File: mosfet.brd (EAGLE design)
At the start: 44.1 x 49.5 mm, 14 parts, among them Q1 BC847CSMD, Q2 BC847CSMD, Q3 BC857CSMD, Q4 IRF530, T1 AO3406, T2 AO3407

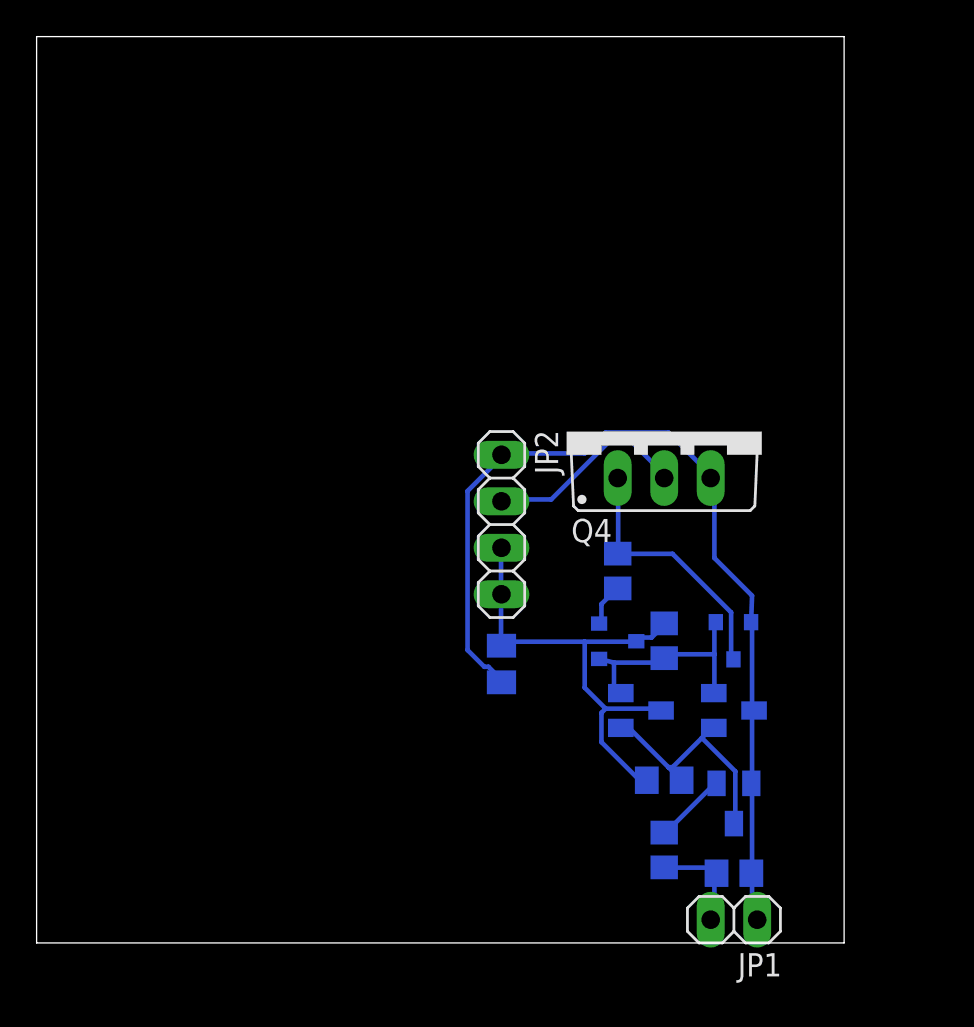
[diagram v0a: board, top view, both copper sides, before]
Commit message: Update mosfet driver to v2
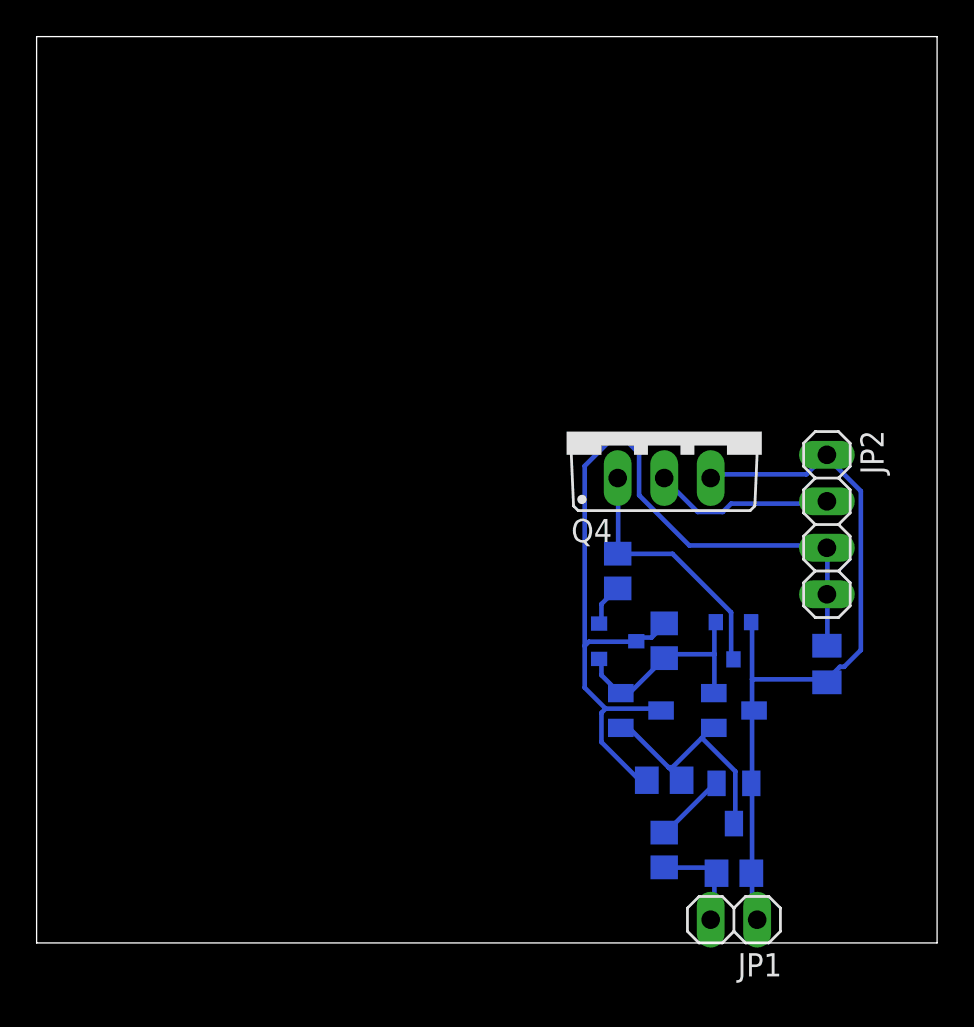
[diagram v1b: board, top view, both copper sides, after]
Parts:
- moved C2 17.8 mm to (43.2, 15.2)
- moved JP2 17.8 mm to (43.2, 22.9)
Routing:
- net N$8: track 27.5 -> 50.1 mm
- net N$3: track 52.5 -> 41.6 mm
- net N$10: track 11.2 -> 9.90 mm
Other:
- board size 44.1 x 49.5 mm -> 49.2 x 49.5 mm

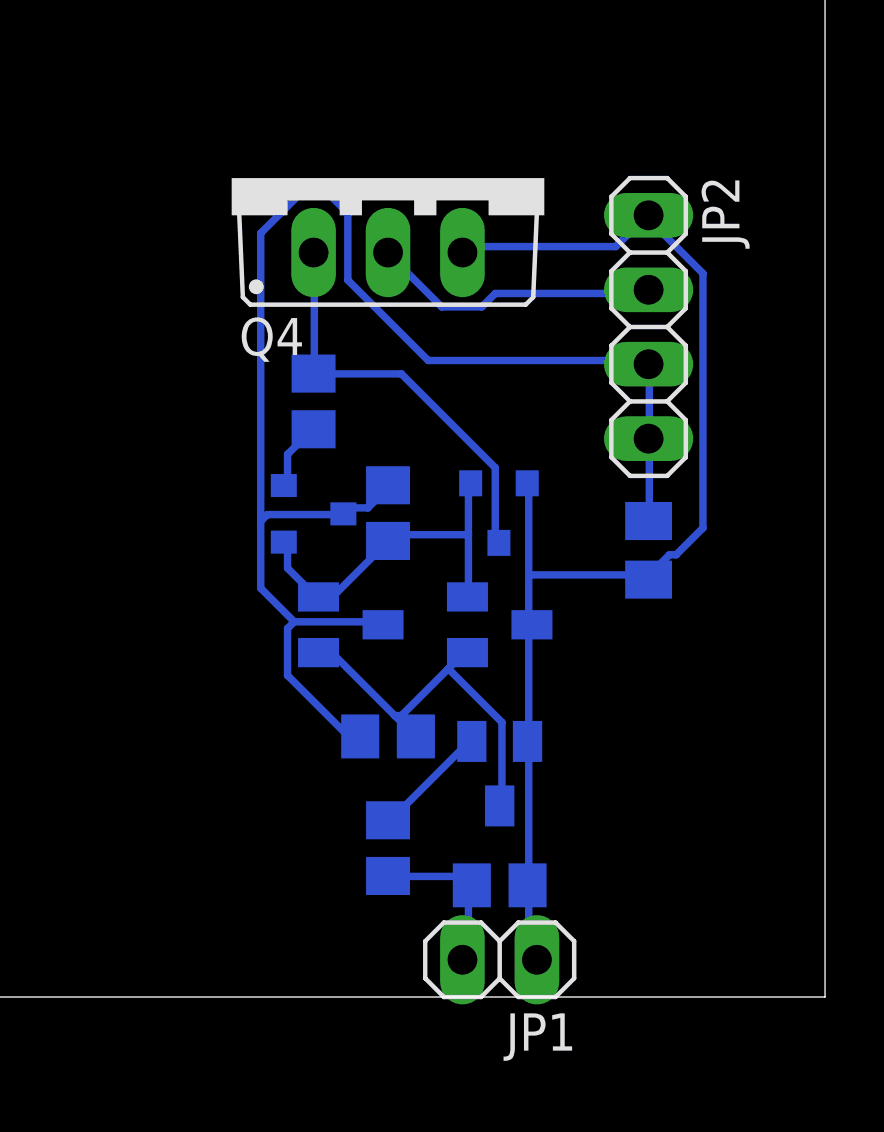
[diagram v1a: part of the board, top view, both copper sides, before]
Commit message: Update mosfet driver to v3
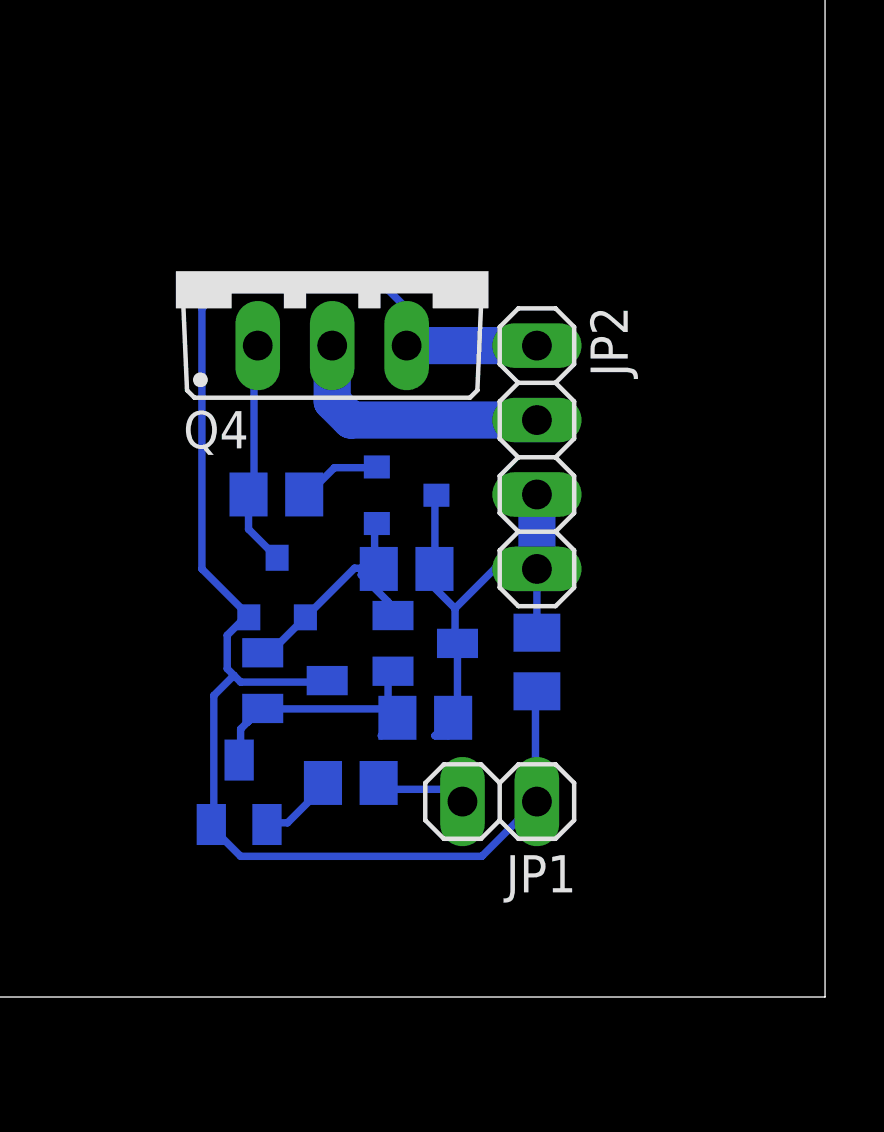
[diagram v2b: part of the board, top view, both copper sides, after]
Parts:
- removed R3: 100k, rcl:R0805
- moved Q2 8.91 mm to (29.2, 6.99), turned to 0 degrees
- moved T1 8.03 mm to (30.5, 14.0), turned to 180 degrees
- moved Q3 7.24 mm to (31.1, 10.8)
- moved JP2 5.85 mm to (39.4, 18.4)
- moved JP1 5.40 mm to (38.1, 6.67)
- moved C2 5.39 mm to (39.4, 11.4)
- moved Q4 3.70 mm to (32.4, 24.8)
- moved R5 3.42 mm to (30.5, 17.1), turned to 180 degrees
- moved T2 3.24 mm to (34.9, 17.1)
- moved Q1 2.62 mm to (35.6, 12.1)
- moved R2 2.56 mm to (33.0, 7.30), turned to 0 degrees
- moved R4 2.01 mm to (34.9, 14.6), turned to 180 degrees
- moved R1 1.42 mm to (35.6, 9.53), turned to 180 degrees
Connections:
- net N$3: no longer R3.1
- net N$5: no longer R3.2
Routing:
- net N$8: track 50.1 -> 19.6 mm
- net N$3: track 41.6 -> 52.5 mm
- net N$1: track 14.3 -> 7.84 mm
- net N$6: track 13.3 -> 10.3 mm
- net N$5: track 5.70 -> 3.26 mm
- net N$7: track 12.4 -> 10.1 mm
- net N$4: track 4.09 -> 2.59 mm
- net N$10: track 9.90 -> 9.15 mm
- net N$2: track 2.35 -> 2.86 mm

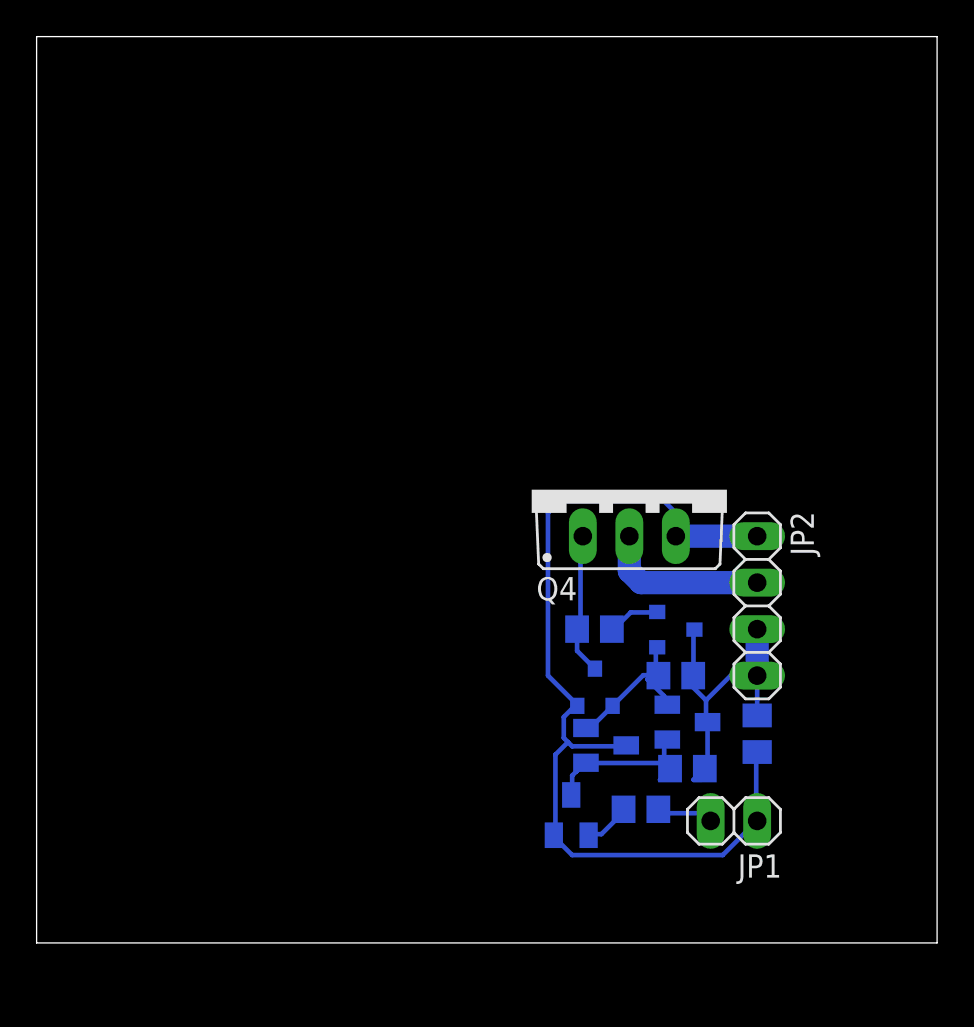
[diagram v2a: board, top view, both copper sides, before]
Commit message: Update mosfet driver to v4
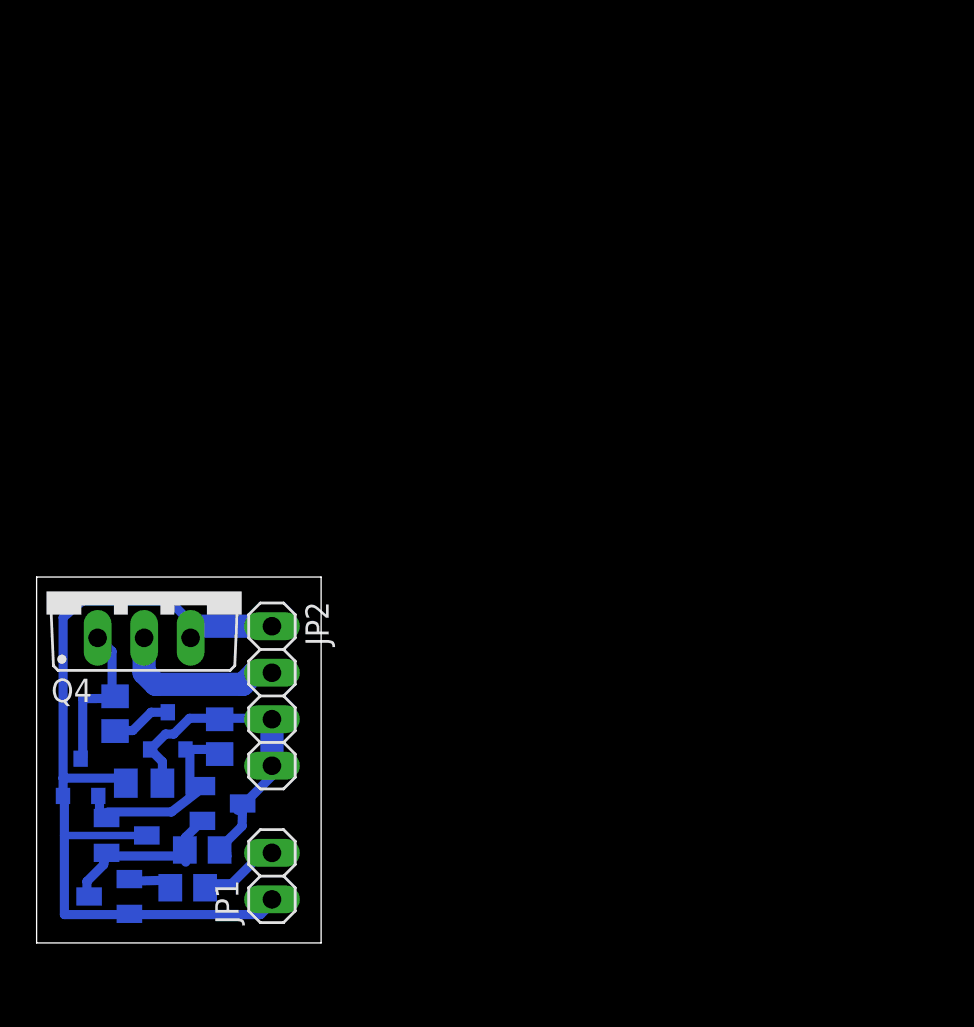
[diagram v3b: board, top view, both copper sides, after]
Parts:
- moved C2 33.6 mm to (5.87, 8.73), turned to 0 degrees
- moved T1 28.5 mm to (2.38, 9.05)
- moved T2 28.3 mm to (7.14, 11.6), turned to 180 degrees
- moved Q4 27.1 mm to (5.87, 19.2)
- moved JP2 27.0 mm to (12.9, 13.5)
- moved R1 26.9 mm to (9.05, 5.08)
- moved Q3 26.7 mm to (4.92, 5.87)
- moved R5 26.6 mm to (4.29, 12.5), turned to 270 degrees
- moved Q1 25.8 mm to (10.2, 7.62)
- moved Q2 25.6 mm to (3.97, 2.54), turned to 270 degrees
- moved JP1 25.4 mm to (12.9, 3.65), turned to 90 degrees
- moved R4 25.1 mm to (10.0, 11.3), turned to 90 degrees
- moved R2 25.1 mm to (8.26, 3.02)
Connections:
- net N$2: now also T2.1; no longer T2.2
- net N$8: now also T2.2; no longer T2.1
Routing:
- net N$7: track 10.1 -> 12.6 mm
- net N$3: track 52.5 -> 50.5 mm
- net N$6: track 10.3 -> 12.0 mm
- net N$5: track 3.26 -> 4.72 mm
- net N$1: track 7.84 -> 8.79 mm
- net N$8: track 19.6 -> 20.4 mm
- net N$4: track 2.59 -> 3.14 mm
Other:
- board size 49.2 x 49.5 mm -> 15.5 x 20 mm

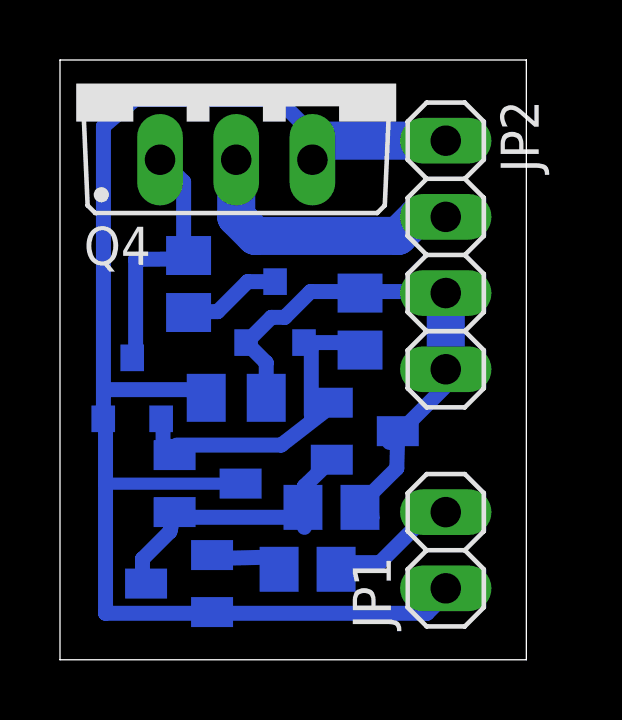
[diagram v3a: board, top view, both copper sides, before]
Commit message: Update mosfet driver to v5
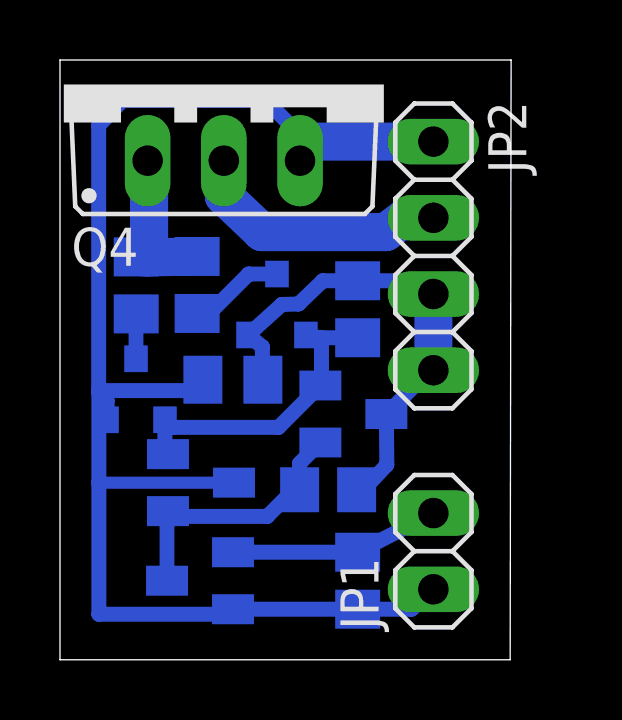
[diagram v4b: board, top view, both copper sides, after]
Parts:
- removed Q2: BC847CSMD, transistor-npn:SOT23
- added R3: 22, rcl:R0805
- added T3: 2N7002E, nxp_60:SOT23
- R2: value 1k -> 100k
- R5: value 10 -> 22
- moved R2 1.71 mm to (9.92, 2.64), turned to 270 degrees
- moved Q1 0.69 mm to (9.78, 8.19)
- moved C2 0.61 mm to (5.76, 9.33)
- moved R1 0.60 mm to (8.94, 5.67)
- moved R4 0.42 mm to (9.92, 11.7)
- moved JP1 0.41 mm to (12.4, 3.62)
- moved JP2 0.41 mm to (12.4, 13.5)
- moved Q4 0.41 mm to (5.46, 19.2)
- moved R5 0.29 mm to (4.57, 12.5)
- moved T2 0.26 mm to (7.21, 11.8)
- moved Q3 0.22 mm to (4.70, 5.91)
- moved T1 0.13 mm to (2.51, 9.02)
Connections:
- removed net N$4: Q2.1, R2.2
- new net N$9: R3.2, T1.1
- net N$1: now also R3.1; no longer T1.1
- net N$3: now also R2.2, T3.2; no longer Q2.2
- net N$5: now also T3.1
- net N$6: now also T3.3; no longer Q2.3
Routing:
- net N$8: track 20.4 -> 16.7 mm
- net N$4: track 3.14 -> 0.00 mm
- net N$1: track 8.79 -> 5.66 mm
- net N$6: track 12.0 -> 9.31 mm
- net N$5: track 4.72 -> 7.00 mm
- net N$7: track 12.6 -> 10.4 mm
- net N$9: track 0.00 -> 1.49 mm
- net N$10: track 9.42 -> 8.80 mm
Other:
- board size 15.5 x 20 mm -> 15 x 20 mm
